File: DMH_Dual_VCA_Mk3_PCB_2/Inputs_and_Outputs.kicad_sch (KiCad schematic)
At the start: 21 parts, among them J0 Conn_01x01, J1 TS_Jack_6.35mm_Sw, J2 TS_Jack_6.35mm_Sw, J200 IDC_02x05, J3 TS_Jack_6.35mm_Sw, J4 TS_Jack_6.35mm_Sw, J5 TS_Jack_6.35mm_Sw, J50 Conn_01x08, J6 TS_Jack_6.35mm_Sw, J60 Conn_01x08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

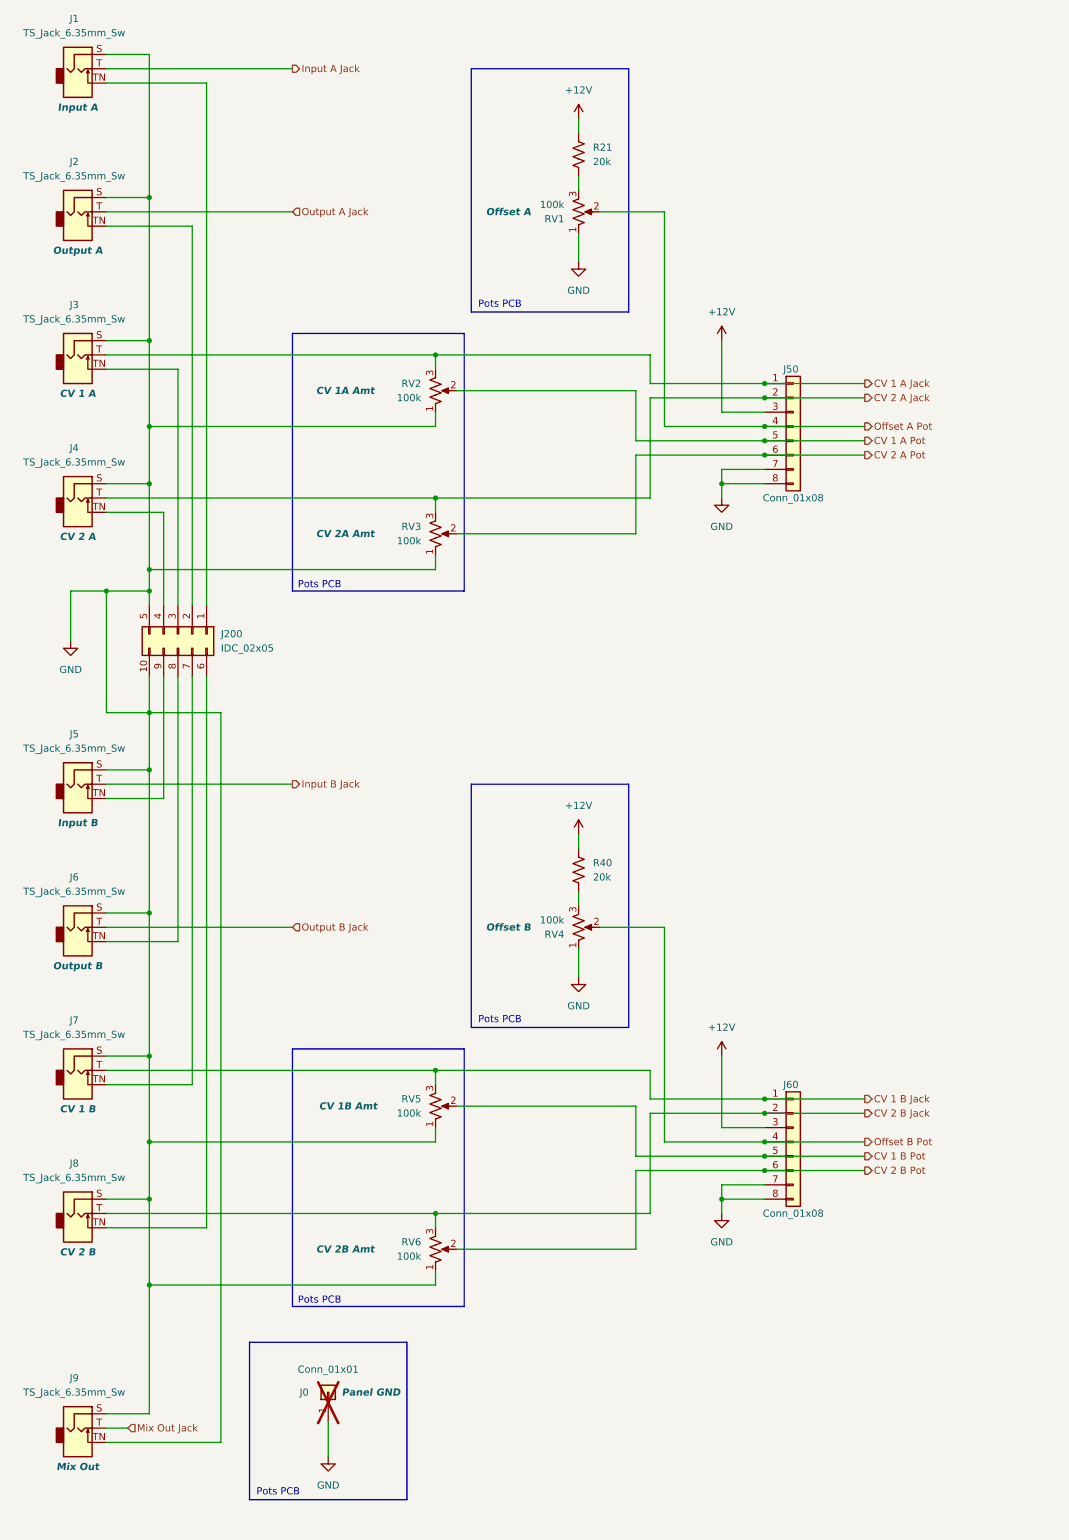
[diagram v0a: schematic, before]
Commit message: Synced PCB 1 and 2 schematics
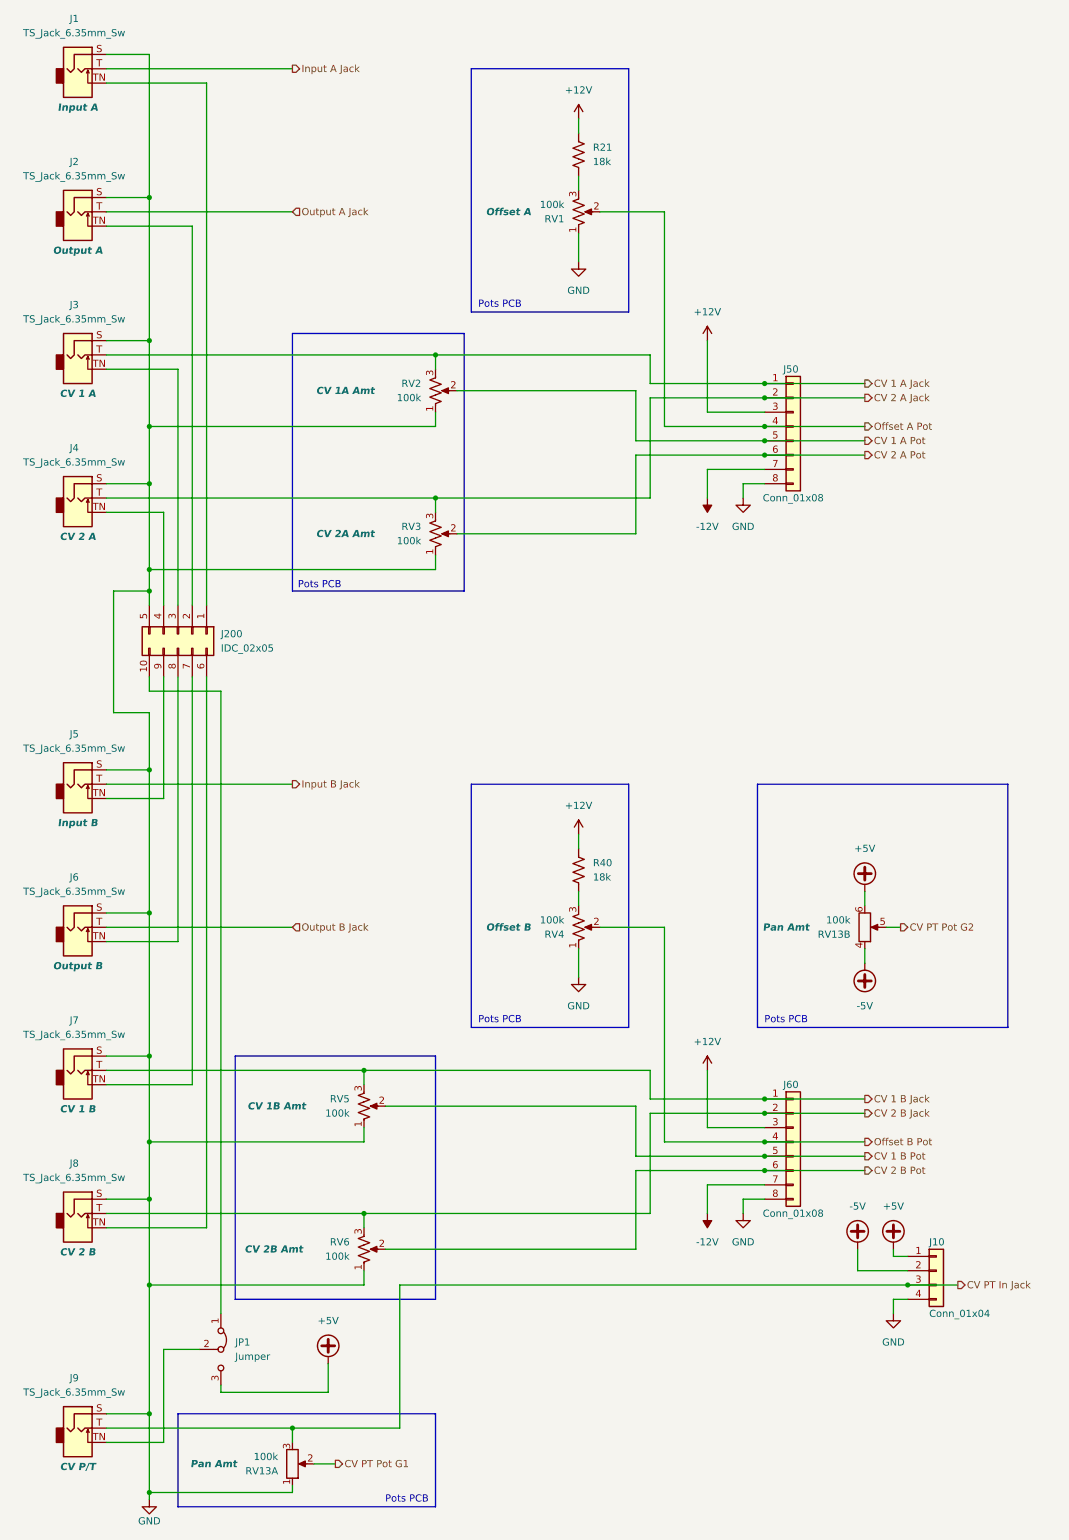
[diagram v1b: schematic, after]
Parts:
- removed J0: Conn_01x01, Connector_PinHeader_2.54mm:PinHeader_1x01_P2.54mm_Vertical, symbol Connector_Generic:Conn_01x01
- added J10: Conn_01x04, Connector_PinSocket_2.54mm:PinSocket_1x04_P2.54mm_Vertical, symbol Connector_Generic:Conn_01x04
- added JP1: Jumper, symbol Jumper:Jumper_3_Bridged12
- added RV13: 100k, SynthStuff:Potentiometer_TT_P110KH1, symbol Device:R_Potentiometer_Dual_Separate
- J50, J60: footprint Connector_PinHeader_2.54mm:PinHeader_1x08_P2.54mm_Vertical -> Connector_PinSocket_2.54mm:PinSocket_1x08_P2.54mm_Vertical
- J9: Function Mix Out -> CV P/T
- R21, R40: value 20k -> 18k
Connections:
- net GND: now also J10.4 (Pin_4), RV13.1; no longer J200.10 (Pin_10), J50.7 (Pin_7), J60.7 (Pin_7), J9.TN
- net Mix Out Jack renamed CV PT In Jack
- net CV PT In Jack: now also J10.3 (Pin_3), RV13.3
- new net: J9.TN, JP1.2 (C)
- new net: J200.10 (Pin_10), JP1.1 (A)
- new net +5V: J10.1 (Pin_1), JP1.3 (B), RV13.6
- new net -12V: J50.7 (Pin_7), J60.7 (Pin_7)
- new net -5V: J10.2 (Pin_2), RV13.4
- new net CV PT Pot G1: RV13.2
- new net CV PT Pot G2: RV13.5
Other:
- moved on the sheet: RV5, RV6

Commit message: Added clipping LED to schematic
Still need to add to Panel
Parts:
- RV13: footprint SynthStuff:Potentiometer_TT_P110KH1 -> Potentiometer_THT:Potentiometer_Alpha_RD902F-40-00D_Dual_Vertical
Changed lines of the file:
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@@
 			)
 		)
-		(property "Footprint" "SynthStuff:Potentiometer_TT_P110KH1"
+		(property "Footprint" "Potentiometer_THT:Potentiometer_Alpha_RD902F-40-00D_Dual_Vertical"
 			(at 165.1 177.8 0)
 			(effects
@@
 			)
 		)
-		(property "Footprint" "SynthStuff:Potentiometer_TT_P110KH1"
+		(property "Footprint" "Potentiometer_THT:Potentiometer_Alpha_RD902F-40-00D_Dual_Vertical"
 			(at 63.5 273.05 0)
 			(effects

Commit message: Positioned controls on PCB 2
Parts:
- RV13: value 100k -> 50k; footprint Potentiometer_THT:Potentiometer_Alpha_RD902F-40-00D_Dual_Vertical -> Potentiometer_THT:Potentiometer_Alps_RK09L_Double_Vertical
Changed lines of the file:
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@@
 			)
 		)
-		(property "Value" "100k"
+		(property "Value" "50k"
 			(at 162.56 176.5301 0)
 			(effects
@@
 			)
 		)
-		(property "Footprint" "Potentiometer_THT:Potentiometer_Alpha_RD902F-40-00D_Dual_Vertical"
+		(property "Footprint" "Potentiometer_THT:Potentiometer_Alps_RK09L_Double_Vertical"
 			(at 165.1 177.8 0)
 			(effects
@@
 			)
 		)
-		(property "Value" "100k"
+		(property "Value" "50k"
 			(at 60.96 271.7801 0)
 			(effects
@@
 			)
 		)
-		(property "Footprint" "Potentiometer_THT:Potentiometer_Alpha_RD902F-40-00D_Dual_Vertical"
+		(property "Footprint" "Potentiometer_THT:Potentiometer_Alps_RK09L_Double_Vertical"
 			(at 63.5 273.05 0)
 			(effects
